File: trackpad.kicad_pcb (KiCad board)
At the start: 2 copper layers, 172 x 152.9 mm, 103 parts, among them J1 USB_C_Receptacle_USB2.0, J3 Conn_01x03, J5 Conn_01x07_Pin, J6 Conn_01x04_Pin, J7 Conn_01x02_Pin, J8 Conn_01x08_Pin, SW1 RotaryEncoder_Switch, SW2 SW_Push, SW3 SW_Push, SW4 SW_Push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

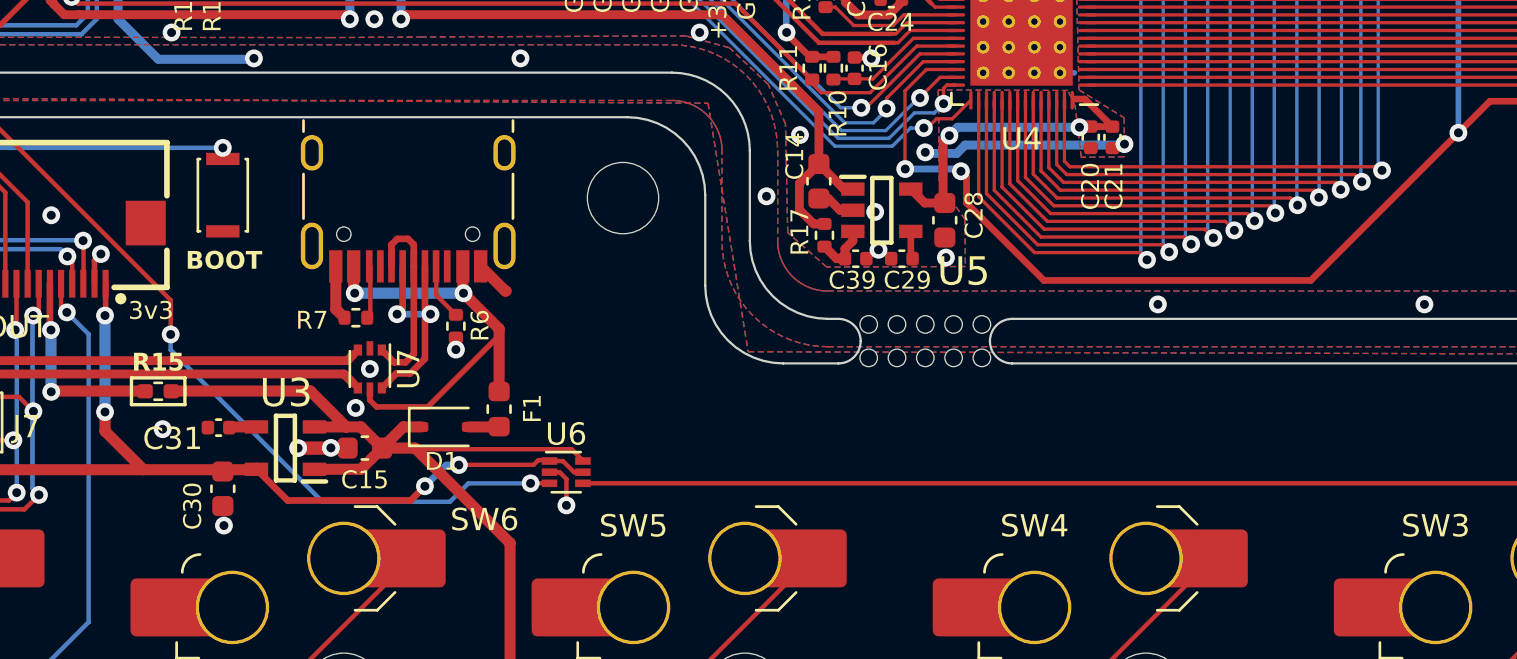
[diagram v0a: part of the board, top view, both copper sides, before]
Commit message: Switch LDO for a cheaper part.
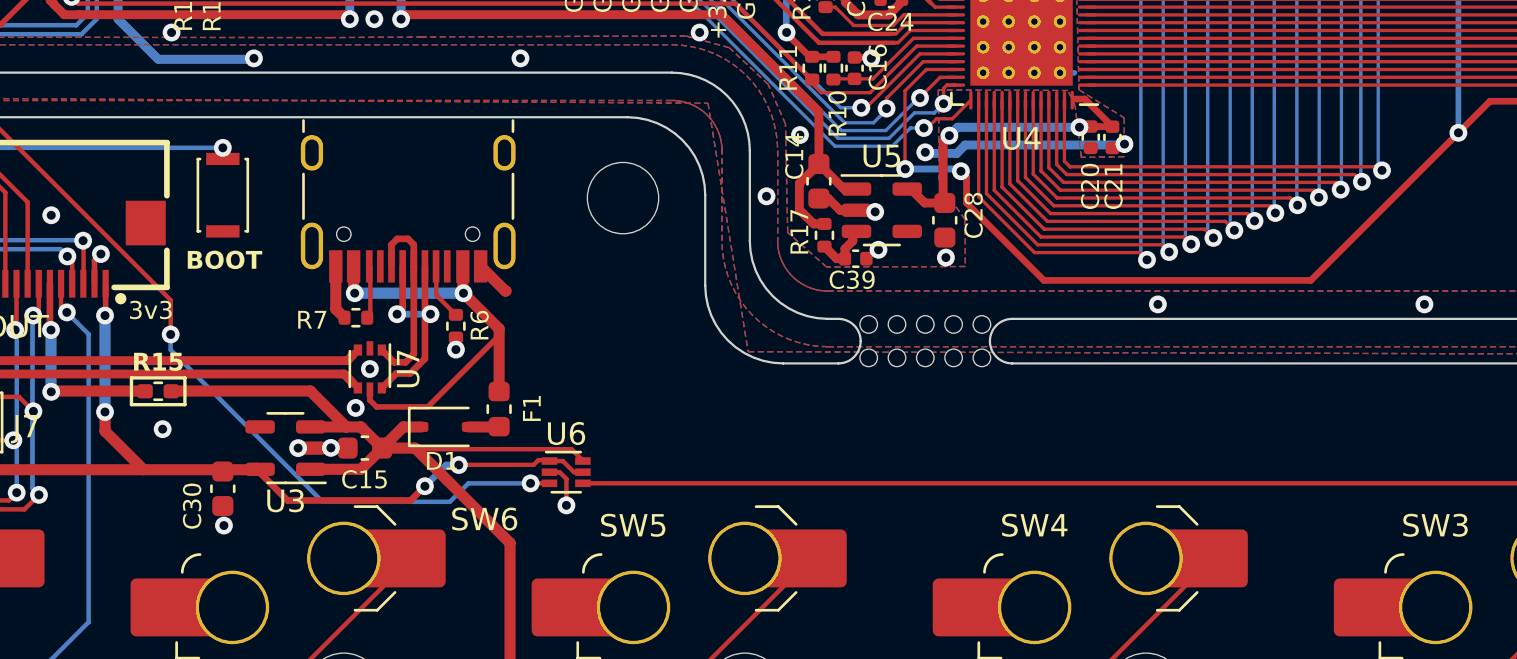
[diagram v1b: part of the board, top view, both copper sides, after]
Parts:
- removed C29, C31: 100n, Capacitor_SMD:C_0402_1005Metric
- C14, C15, C28, C30: value 2.2µ -> 1µ
- U3, U5: footprint Trackpad:SOT95P280X100-5N -> Package_TO_SOT_SMD:SOT-23-5
- U4: value ~ -> mXT336UD-MAU002
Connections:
- U3 pad 4: Net-(U3-BYP) -> unconnected-(U3-NC-Pad4)
- U5 pad 4: Net-(U5-BYP) -> unconnected-(U5-NC-Pad4)
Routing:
- net Net-(U3-BYP): track 1.24 -> 0.00 mm
- net Net-(U5-BYP): track 1.15 -> 0.00 mm

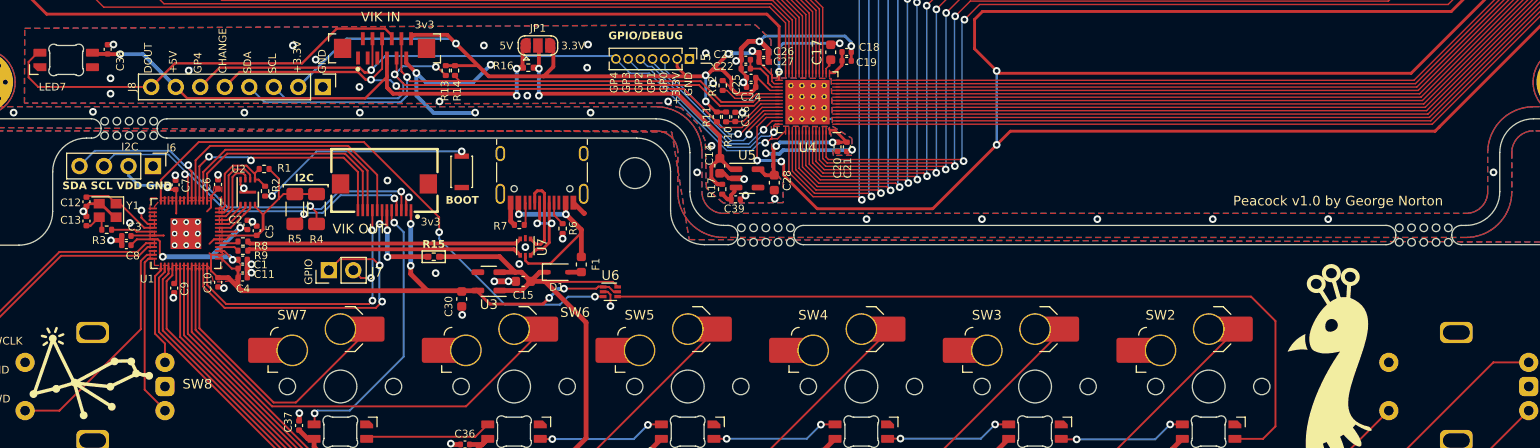
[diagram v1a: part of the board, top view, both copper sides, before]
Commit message: Move USB port closer to the edge, Additional silkscreen, Add reset header, shrink LDO caps, swap QSPI flash.
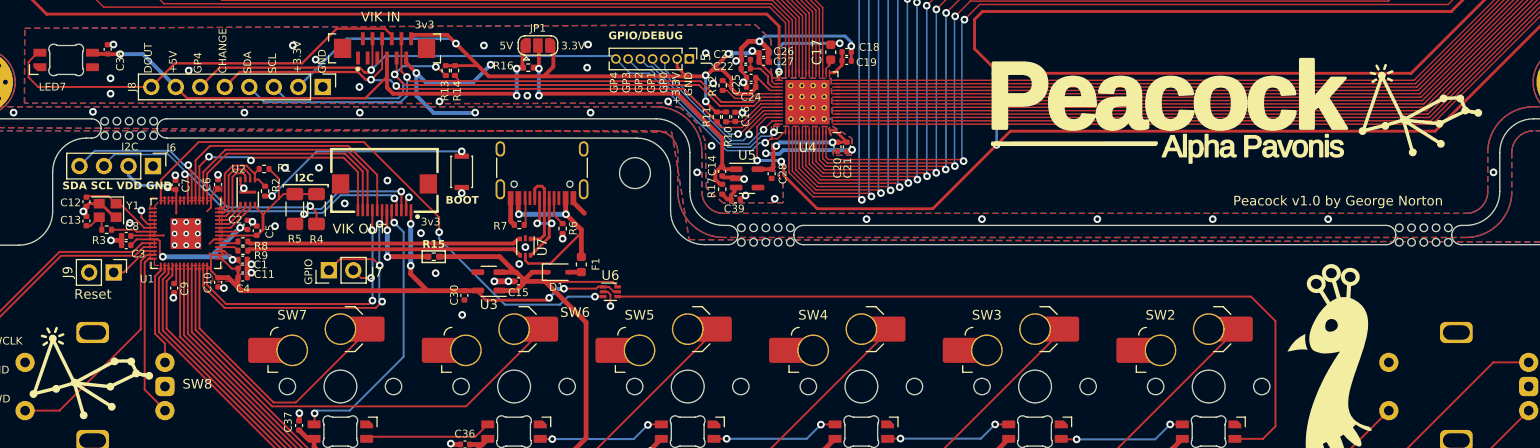
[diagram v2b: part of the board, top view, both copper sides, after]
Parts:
- added J9: Conn_01x02_Pin, Connector_PinHeader_2.54mm:PinHeader_1x02_P2.54mm_Vertical, F.Cu at (32.3, 186.4)
- C14, C15, C28, C30: footprint Capacitor_SMD:C_0603_1608Metric -> Capacitor_SMD:C_0402_1005Metric
- U2: value GD25Q80CEIGR -> W25Q16JVUXIQ
- moved C28 0.97 mm to (100.5, 176.2)
- moved C14 0.63 mm to (95.4, 175.9)
- moved C15 0.50 mm to (74.3, 187.3)
- moved J1 0.47 mm to (76.7, 174.7)
- moved C30 0.47 mm to (68.7, 188.8)
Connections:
- J1 pad A6: Net-(J1-D+-PadA6) -> /Macropad/D+
- J1 pad A7: Net-(J1-D--PadA7) -> /Macropad/D-
- J1 pad B6: Net-(J1-D+-PadA6) -> /Macropad/D+
- J1 pad B7: Net-(J1-D--PadA7) -> /Macropad/D-
- U1 pad 26: unconnected-(U1-RUN-Pad26) -> /Macropad/RUN
- U7 pad 1: Net-(J1-D+-PadA6) -> /Macropad/D+
- U7 pad 6: Net-(J1-D--PadA7) -> /Macropad/D-
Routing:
- net /Macropad/D-: track 28.6 -> 39.5 mm, vias 0 -> 2
- net Net-(J1-D--PadA7): track 10.4 -> 0.00 mm, vias 2 -> 0
- net Net-(J1-D+-PadA6): track 8.91 -> 0.00 mm
- net /Macropad/D+: track 28.7 -> 36.9 mm
- net /Macropad/RUN: track 0.00 -> 4.97 mm
- net Net-(JP1-C): track 34.7 -> 33.5 mm
- net +3.3VA: track 14.2 -> 13.0 mm
- net +5V: track 157.3 -> 158.4 mm
- net VBUS: track 20.4 -> 21.4 mm
- net GND: track 29.1 -> 30.0 mm, vias 33 -> 39
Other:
- board text added: "Reset"

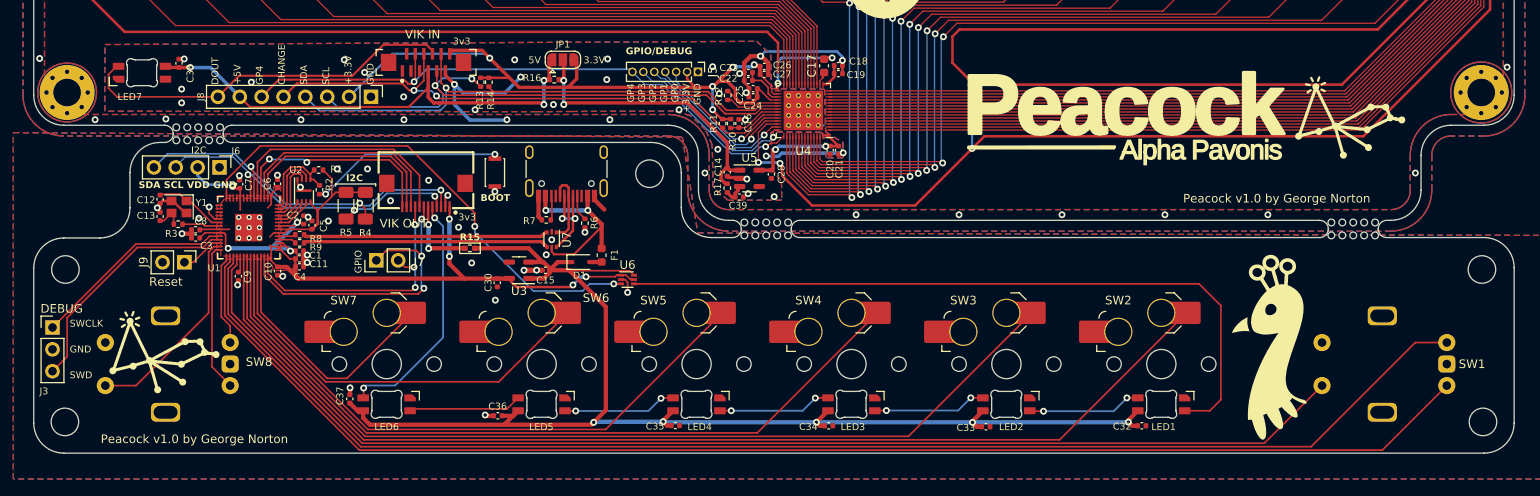
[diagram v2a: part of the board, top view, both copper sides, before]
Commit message: Re-route to avoid crossing the USB data lines. Reduced keys to 5 to avoid having to route a long trace around the crystal, swaped key footprint from choc hotswap to mx/choc combined soldered.
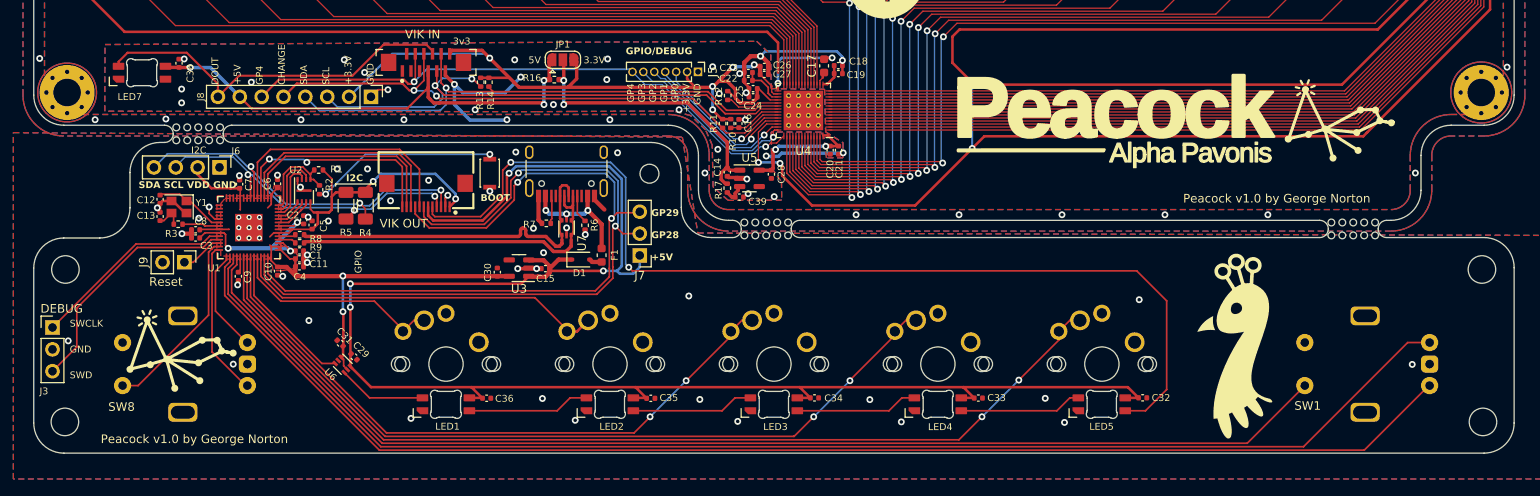
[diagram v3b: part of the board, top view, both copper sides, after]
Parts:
- removed C37: 100n, Capacitor_SMD:C_0402_1005Metric
- removed LED6: SK6812-MINI-E, PCM_marbastlib-various:LED_6028R
- removed R15: 0k, Resistor_SMD:R_0402_1005Metric_Pad0.72x0.64mm_HandSolder
- removed SW7: SW_Push, PCM_marbastlib-choc:SW_choc_v1_HS_1u
- added C29: 100n, Capacitor_SMD:C_0402_1005Metric, F.Cu at (52.0, 197.4)
- added C31: 100n, Capacitor_SMD:C_0402_1005Metric, F.Cu at (50.4, 195.8)
- H6: footprint MountingHole:MountingHole_3.2mm_M3 -> MountingHole:MountingHole_2.2mm_M2
- J7: footprint Connector_PinHeader_2.54mm:PinHeader_1x02_P2.54mm_Vertical -> Connector_PinHeader_2.54mm:PinHeader_1x03_P2.54mm_Vertical
- R10: value 10k -> 12k
- SW2, SW3, SW4, SW5, SW6: footprint PCM_marbastlib-choc:SW_choc_v1_HS_1u -> PCM_marbastlib-xp-choc:SW_choc_MxCombo_1u; moved to B.Cu
- moved LED1 83.1 mm to (62.7, 202.9), turned to 0 degrees
- moved LED5 65.1 mm to (138.9, 202.9), turned to 0 degrees
- moved LED2 46.1 mm to (81.8, 202.9), turned to 0 degrees
- moved U6 34.5 mm to (50.7, 198.4), turned to -45 degrees
- moved J7 30.6 mm to (85.2, 185.6), turned to 180 degrees
- moved LED4 28.0 mm to (119.9, 202.9), turned to 0 degrees
- moved SW6 11.1 mm to (62.7, 198.2)
- moved SW5 10.1 mm to (81.8, 198.2)
- moved SW4 9.01 mm to (100.8, 198.2)
- moved LED3 9.01 mm to (100.8, 202.9), turned to 0 degrees
- moved SW3 7.96 mm to (119.9, 198.2)
- moved SW2 6.91 mm to (138.9, 198.2)
- moved C35 4.26 mm to (86.5, 202.2)
- moved C34 3.64 mm to (105.5, 202.2)
- moved C33 3.44 mm to (124.6, 202.2)
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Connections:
- J2 pad 6: Net-(J2-5V) -> +5V
- J7 pad 1: /Macropad/GPIO_AD1 -> +5V
- J7 pad 2: /Macropad/GPIO_AD2 -> /Macropad/GPIO_AD1
- LED5 pad 2: Net-(LED5-DOUT) -> /Macropad/VIK_RGB
- U1 pad 14: /Macropad/LED_3.3V -> unconnected-(U1-GPIO11-Pad14)
- U1 pad 37: /Macropad/SW5 -> /Macropad/LED_3.3V
- U1 pad 39: /Macropad/SW7 -> /Macropad/SW5
- U7 pad 3: /Macropad/D+ -> /Macropad/D-
- U7 pad 6: /Macropad/D- -> /Macropad/D+
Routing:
- net /Macropad/VIK_RGB: track 28.5 -> 119.3 mm
- net Net-(LED1-DIN): track 84.9 -> 10.3 mm
- net /Macropad/GPIO_AD2: track 31.7 -> 86.7 mm, vias 3 -> 2
- net /Macropad/GPIO_AD1: track 37.5 -> 87.4 mm, vias 3 -> 2
- net /Macropad/LED_3.3V: track 58.2 -> 17.2 mm, vias 2 -> 0
- net +5V: track 158.4 -> 199.4 mm, vias 5 -> 4
- net /Macropad/SW7: track 30.6 -> 0.00 mm
- net /Macropad/SW5: track 72.5 -> 43.5 mm
- net /Macropad/SW6: track 49.3 -> 25.0 mm
- net /Macropad/SW4: track 91.5 -> 75.2 mm, vias 0 -> 2
- net /Macropad/SW3: track 110.2 -> 95.0 mm, vias 0 -> 2
- net /Macropad/SW2: track 129.0 -> 115.2 mm, vias 0 -> 2
- net Net-(LED5-DOUT): track 13.2 -> 0.00 mm
- net Net-(J2-5V): track 8.99 -> 0.00 mm, vias 2 -> 0
- net VBUS: track 21.4 -> 14.5 mm, vias 2 -> 3
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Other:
- board text added: "GP29 GP28 +5V"
- board text removed: "LED6"
